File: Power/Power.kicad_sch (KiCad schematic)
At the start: 9 parts

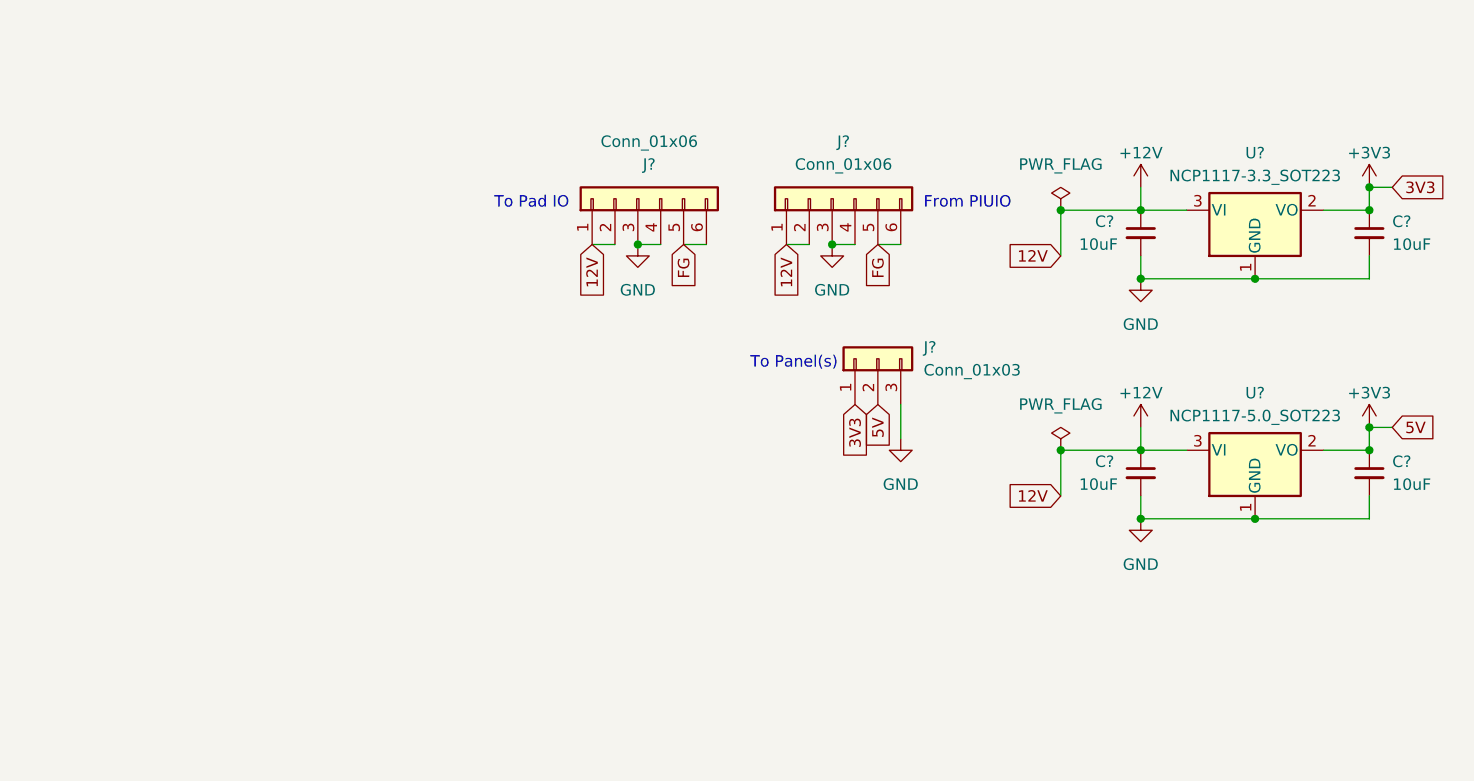
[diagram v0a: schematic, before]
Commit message: Initial power distribution PCB design
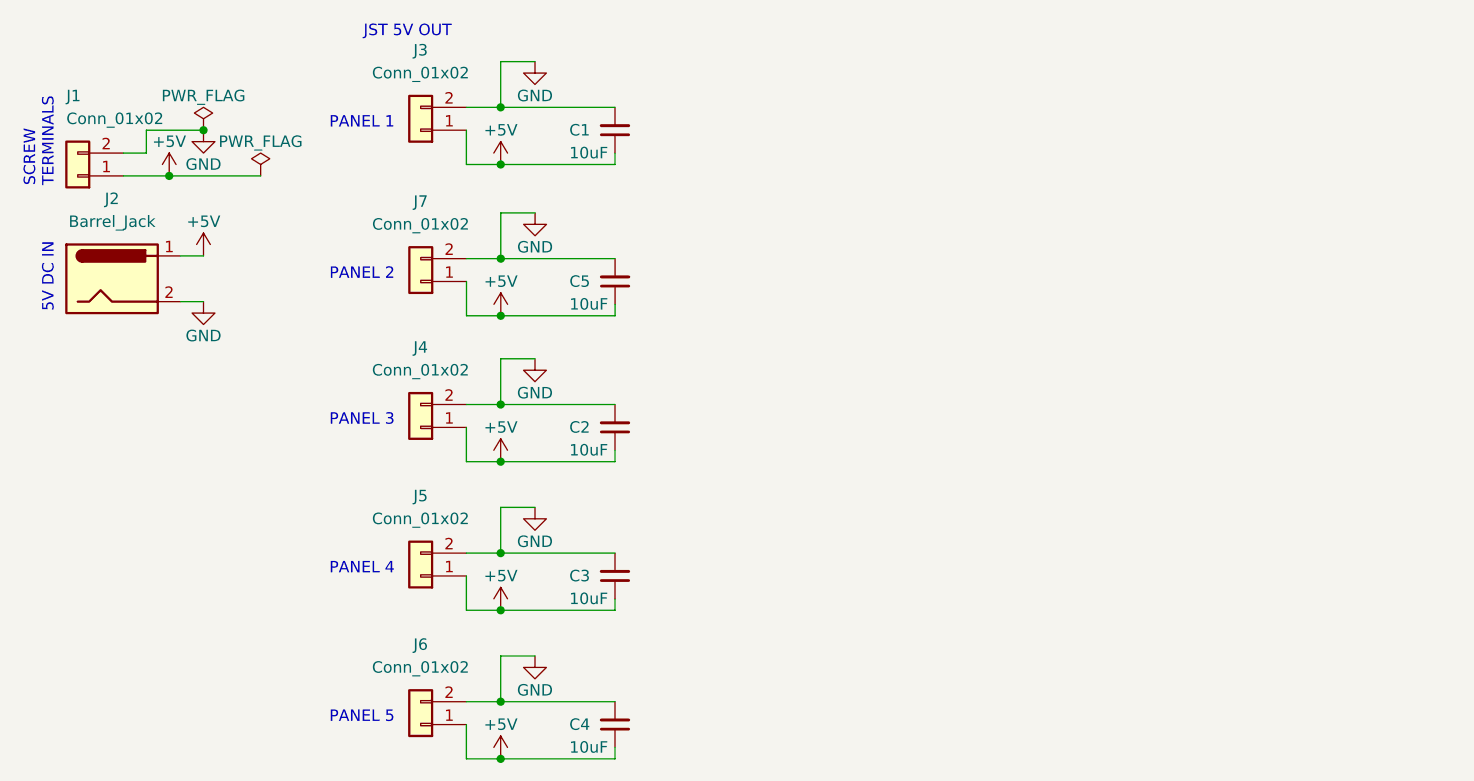
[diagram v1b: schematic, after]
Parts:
- removed C? (x4): 10uF, symbol Device:C_Small
- removed J? (x2): Conn_01x06, symbol Connector_Generic:Conn_01x06
- removed J?: Conn_01x03, symbol Connector_Generic:Conn_01x03
- removed U?: NCP1117-5.0_SOT223, Package_TO_SOT_SMD:SOT-223-3_TabPin2, symbol Regulator_Linear:NCP1117-5.0_SOT223
- removed U?: NCP1117-3.3_SOT223, Package_TO_SOT_SMD:SOT-223-3_TabPin2, symbol Regulator_Linear:NCP1117-3.3_SOT223
- added C1, C2, C3, C4, C5: 10uF, Capacitor_SMD:C_0805_2012Metric_Pad1.18x1.45mm_HandSolder, symbol Device:C_Small
- added J1: Conn_01x02, TerminalBlock:TerminalBlock_bornier-2_P5.08mm, symbol Connector_Generic:Conn_01x02
- added J2: Barrel_Jack, Connector_BarrelJack:BarrelJack_CUI_PJ-063AH_Horizontal, symbol Connector:Barrel_Jack
- added J3, J4, J5, J6, J7: Conn_01x02, Connector_JST:JST_XH_B2B-XH-AM_1x02_P2.50mm_Vertical, symbol Connector_Generic:Conn_01x02
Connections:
- net GND: now also C1.2, C2.2, C3.2, C4.2, C5.2, J1.2 (Pin_2), J2.2, J3.2 (Pin_2), J4.2 (Pin_2), J5.2 (Pin_2), J6.2 (Pin_2), J7.2 (Pin_2)
- new net +5V: C1.1, C2.1, C3.1, C4.1, C5.1, J1.1 (Pin_1), J2.1, J3.1 (Pin_1), J4.1 (Pin_1), J5.1 (Pin_1), J6.1 (Pin_1), J7.1 (Pin_1)
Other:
- note added: "5V DC IN"
- note added: "JST 5V OUT"
- note added: "PANEL 1"
- note added: "PANEL 2"
- note added: "PANEL 3"
- note added: "PANEL 4"
- note added: "PANEL 5"
- note added: "SCREW TERMINALS"
- note removed: "From PIUIO"
- note removed: "To Pad IO"
- note removed: "To Panel(s)"

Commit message: Update power distribution PCB
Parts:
- J3, J4, J5, J6, J7: footprint Connector_JST:JST_XH_B2B-XH-AM_1x02_P2.50mm_Vertical -> Connector_JST:JST_XH_B2B-XH-A_1x02_P2.50mm_Vertical
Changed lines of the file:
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@@
     (property "Reference" "J3" (id 0) (at 86.36 29.21 0))
     (property "Value" "Conn_01x02" (id 1) (at 86.36 31.75 0))
-    (property "Footprint" "Connector_JST:JST_XH_B2B-XH-AM_1x02_P2.50mm_Vertical" (id 2) (at 86.36 38.1 0)
+    (property "Footprint" "Connector_JST:JST_XH_B2B-XH-A_1x02_P2.50mm_Vertical" (id 2) (at 86.36 38.1 0)
       (effects (font (size 1.27 1.27)) hide)
     )
@@
     (property "Reference" "J7" (id 0) (at 86.3709 46.0204 0))
     (property "Value" "Conn_01x02" (id 1) (at 86.3709 48.5604 0))
-    (property "Footprint" "Connector_JST:JST_XH_B2B-XH-AM_1x02_P2.50mm_Vertical" (id 2) (at 86.3709 54.9104 0)
+    (property "Footprint" "Connector_JST:JST_XH_B2B-XH-A_1x02_P2.50mm_Vertical" (id 2) (at 86.3709 54.9104 0)
       (effects (font (size 1.27 1.27)) hide)
     )
@@
     (property "Reference" "J4" (id 0) (at 86.36 62.23 0))
     (property "Value" "Conn_01x02" (id 1) (at 86.36 64.77 0))
-    (property "Footprint" "Connector_JST:JST_XH_B2B-XH-AM_1x02_P2.50mm_Vertical" (id 2) (at 86.36 71.12 0)
+    (property "Footprint" "Connector_JST:JST_XH_B2B-XH-A_1x02_P2.50mm_Vertical" (id 2) (at 86.36 71.12 0)
       (effects (font (size 1.27 1.27)) hide)
     )
@@
     (property "Reference" "J5" (id 0) (at 86.36 78.74 0))
     (property "Value" "Conn_01x02" (id 1) (at 86.36 81.28 0))
-    (property "Footprint" "Connector_JST:JST_XH_B2B-XH-AM_1x02_P2.50mm_Vertical" (id 2) (at 86.36 87.63 0)
+    (property "Footprint" "Connector_JST:JST_XH_B2B-XH-A_1x02_P2.50mm_Vertical" (id 2) (at 86.36 87.63 0)
       (effects (font (size 1.27 1.27)) hide)
     )
@@
     (property "Reference" "J6" (id 0) (at 86.36 95.25 0))
     (property "Value" "Conn_01x02" (id 1) (at 86.36 97.79 0))
-    (property "Footprint" "Connector_JST:JST_XH_B2B-XH-AM_1x02_P2.50mm_Vertical" (id 2) (at 86.36 104.14 0)
+    (property "Footprint" "Connector_JST:JST_XH_B2B-XH-A_1x02_P2.50mm_Vertical" (id 2) (at 86.36 104.14 0)
       (effects (font (size 1.27 1.27)) hide)
     )
@@
     )
     (path "/006d3987-f9df-472e-9bbe-1bfc11d06c24"
-      (reference "J3") (unit 1) (value "Conn_01x02") (footprint "Connector_JST:JST_XH_B2B-XH-AM_1x02_P2.50mm_Vertical")
+      (reference "J3") (unit 1) (value "Conn_01x02") (footprint "Connector_JST:JST_XH_B2B-XH-A_1x02_P2.50mm_Vertical")
     )
     (path "/aa70e224-c2b5-4634-858d-6e9bb2baaa1d"
-      (reference "J4") (unit 1) (value "Conn_01x02") (footprint "Connector_JST:JST_XH_B2B-XH-AM_1x02_P2.50mm_Vertical")
+      (reference "J4") (unit 1) (value "Conn_01x02") (footprint "Connector_JST:JST_XH_B2B-XH-A_1x02_P2.50mm_Vertical")
     )
     (path "/ad7d6d53-548c-41c9-af54-850c08d310ef"
-      (reference "J5") (unit 1) (value "Conn_01x02") (footprint "Connector_JST:JST_XH_B2B-XH-AM_1x02_P2.50mm_Vertical")
+      (reference "J5") (unit 1) (value "Conn_01x02") (footprint "Connector_JST:JST_XH_B2B-XH-A_1x02_P2.50mm_Vertical")
     )
     (path "/db64afda-5818-43ee-a248-004b0895a4d1"
-      (reference "J6") (unit 1) (value "Conn_01x02") (footprint "Connector_JST:JST_XH_B2B-XH-AM_1x02_P2.50mm_Vertical")
+      (reference "J6") (unit 1) (value "Conn_01x02") (footprint "Connector_JST:JST_XH_B2B-XH-A_1x02_P2.50mm_Vertical")
     )
     (path "/21583fc6-ce62-4fe7-a746-4e59e1e19bc3"
-      (reference "J7") (unit 1) (value "Conn_01x02") (footprint "Connector_JST:JST_XH_B2B-XH-AM_1x02_P2.50mm_Vertical")
-    )
-  )
+      (reference "J7") (unit 1) (value "Conn_01x02") (footprint "Connector_JST:JST_XH_B2B-XH-A_1x02_P2.50mm_Vertical")
+    )
+  )
